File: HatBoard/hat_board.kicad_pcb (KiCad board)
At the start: 4 copper layers, 132 x 106.5 mm, 50 parts, among them J1 DF11 FC Connection, J13 DF11 FC Connection, J20 DF11 FC Connection, J21 DF11 FC Connection, J3 Conn_01x04, J4 Conn_01x04, J5 Conn_01x04, J6 Conn_01x04, J7 Conn_01x04, J8 Conn_01x04, U10 VEML7700, U12 DRV2605LDGS, U13 TCA4311A, U17 TCA4311A, U21 TCA4311A, U27 TMP112AIDRLR, U4 TCA4311A, U5 TCA4311A, U9 TCA4311A

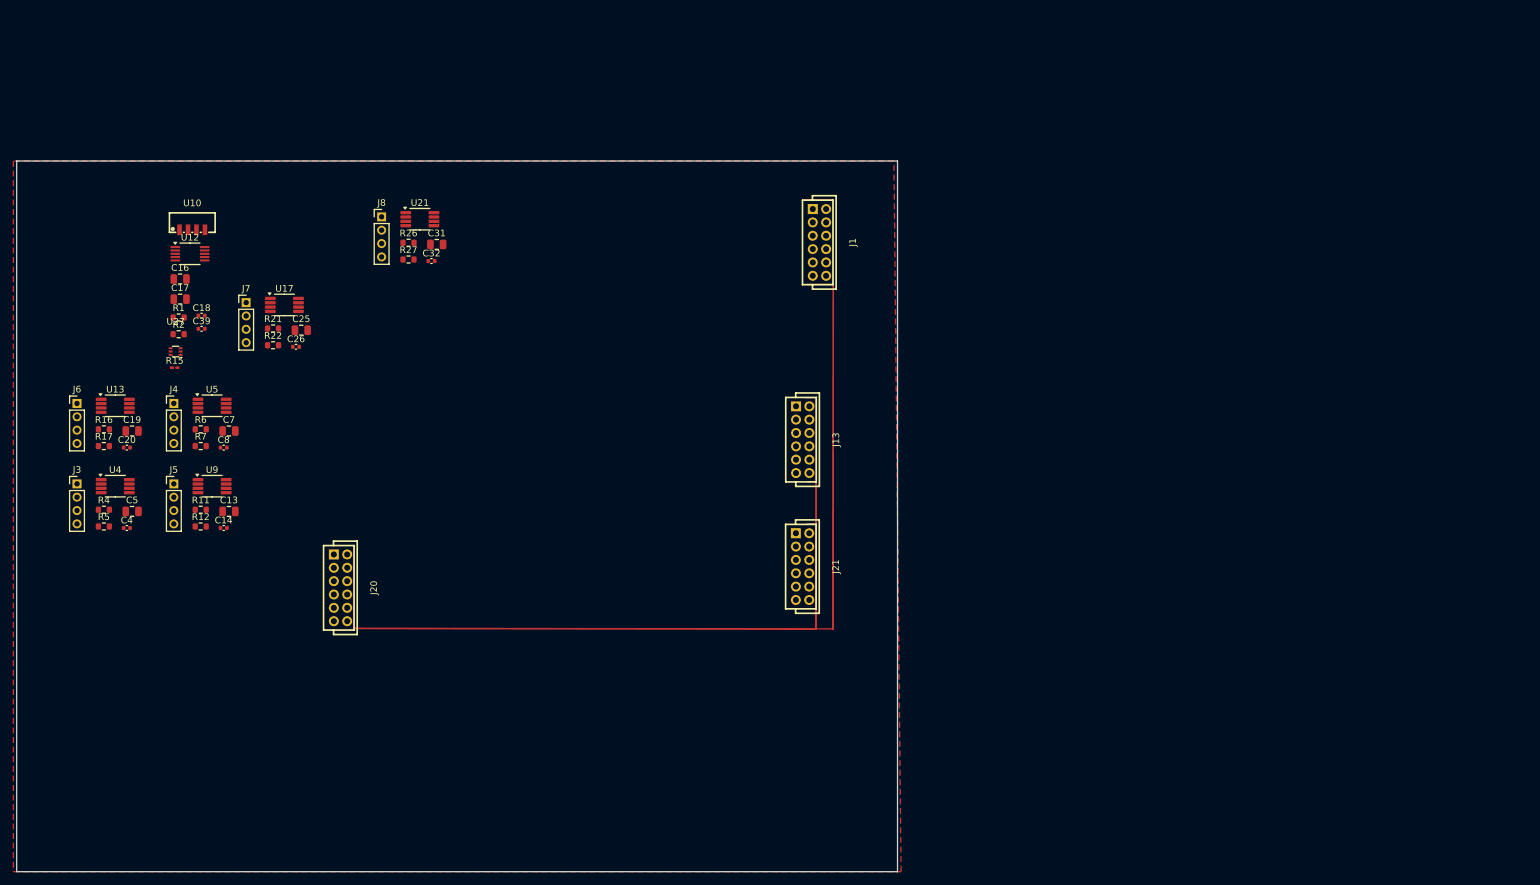
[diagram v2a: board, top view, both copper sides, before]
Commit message: mirror flipped placement
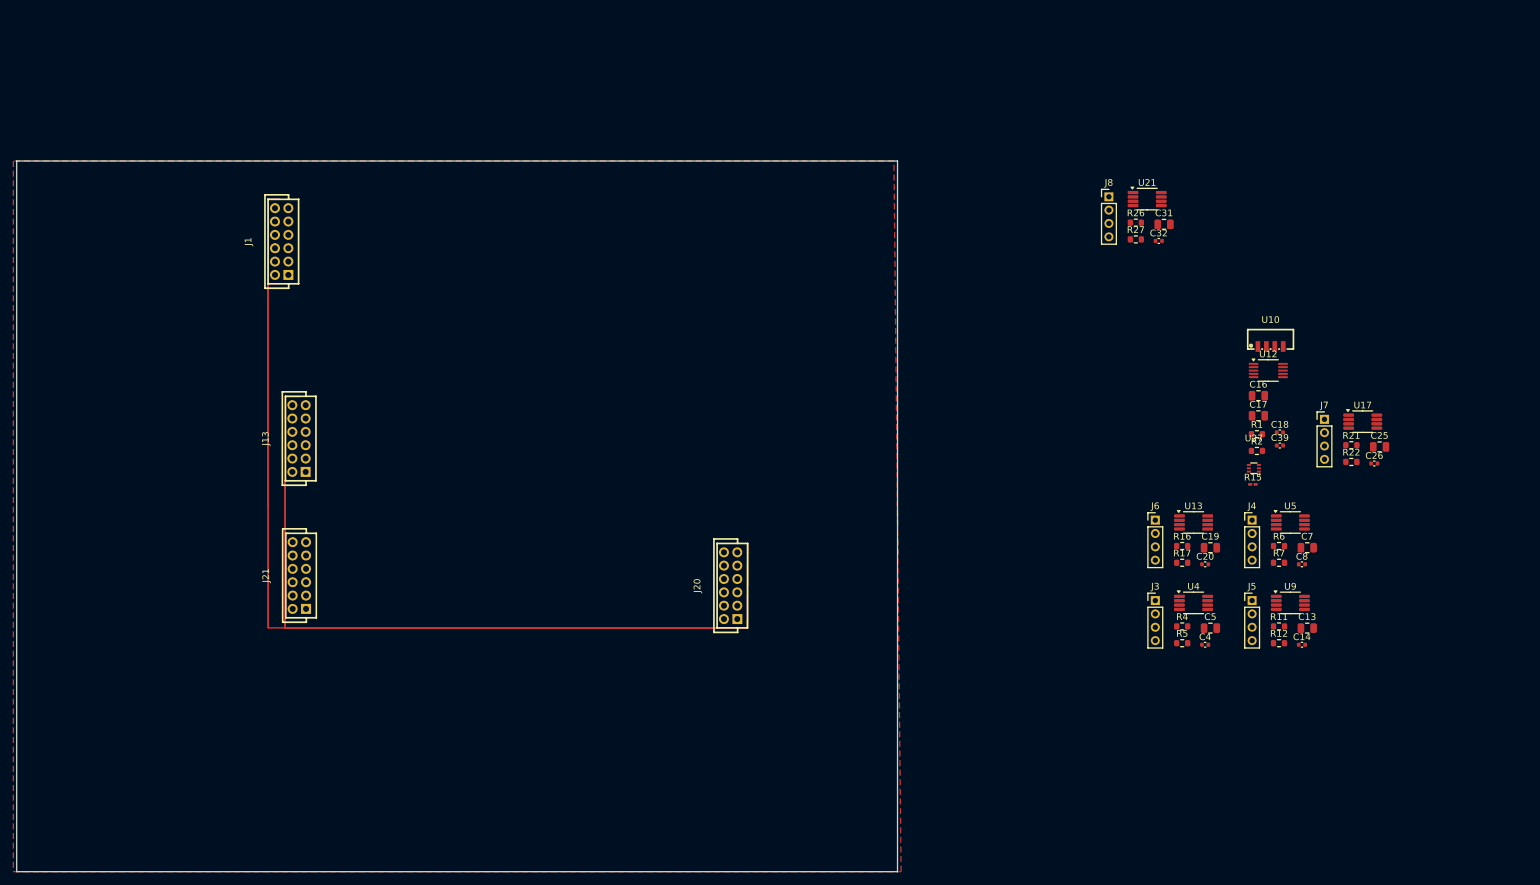
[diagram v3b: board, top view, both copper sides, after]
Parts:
- moved C14 162.5 mm to (223.1, 132.5)
- moved C17 162.5 mm to (216.6, 98.2)
- moved C25 162.5 mm to (234.7, 102.8)
- moved C4 162.5 mm to (208.6, 132.5)
- moved C7 162.5 mm to (223.9, 118.0)
- moved J3 162.5 mm to (201.1, 125.9)
- moved R16 162.5 mm to (205.2, 117.7)
- moved R2 162.5 mm to (216.4, 103.5)
- moved U17 162.5 mm to (232.2, 99.1)
- moved C13 162.5 mm to (223.9, 130.0)
- moved C16 162.5 mm to (216.6, 95.2)
- moved C18 162.5 mm to (219.8, 100.7)
- moved C19 162.5 mm to (209.4, 118.0)
- moved C20 162.5 mm to (208.6, 120.4)
- moved C39 162.5 mm to (219.8, 102.6)
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
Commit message: finihsed connection, need to reroute certain traces ++ double check orientation of connectors
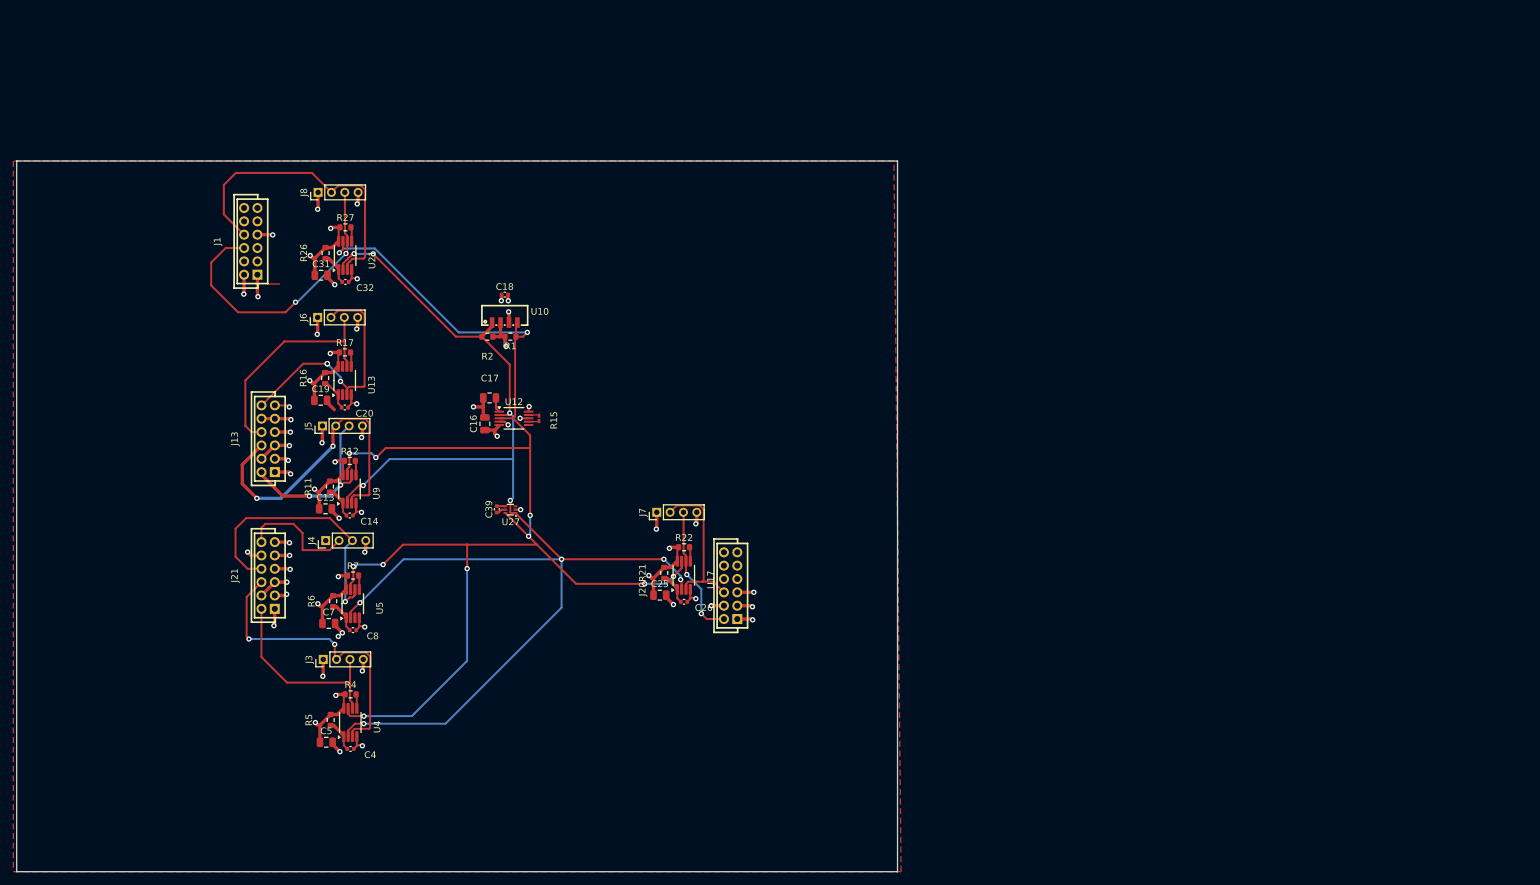
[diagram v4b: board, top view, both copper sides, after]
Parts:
- moved C13 148.2 mm to (76.8, 112.1)
- moved C7 147.1 mm to (77.3, 129.3)
- moved C14 144.0 mm to (80.4, 113.1)
- moved R11 143.8 mm to (77.4, 108.8), turned to -90 degrees
- moved C8 142.6 mm to (80.9, 130.3)
- moved U9 142.0 mm to (80.4, 109.2), turned to 90 degrees
- moved R6 142.0 mm to (77.9, 126.0), turned to -90 degrees
- moved R12 141.9 mm to (80.4, 104.9)
- moved J5 141.8 mm to (76.3, 99.7), turned to 90 degrees
- moved U5 141.0 mm to (80.9, 126.3), turned to 90 degrees
- moved J4 138.9 mm to (76.8, 116.9), turned to 90 degrees
- moved R7 138.8 mm to (80.9, 122.1)
- moved C19 135.1 mm to (76.1, 95.9)
- moved C5 133.6 mm to (76.9, 147.1)
- moved C20 131.1 mm to (79.7, 96.9)
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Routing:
- net SDA: track 0.00 -> 209.4 mm, vias 0 -> 12
- net SCL: track 0.00 -> 203.5 mm, vias 0 -> 10
- net +3V3: track 0.00 -> 109.5 mm, vias 0 -> 25
- net GND: track 0.00 -> 91.3 mm, vias 0 -> 40
- net /SCLIN: track 0.00 -> 68.1 mm, vias 0 -> 2
- net /SDAIN: track 0.00 -> 66.6 mm, vias 0 -> 2
- net /SCLIN_F3: track 0.00 -> 48.0 mm, vias 0 -> 2
- net /SCLIN_F1: track 0.00 -> 45.2 mm, vias 0 -> 2
- net /SDAIN_F2: track 0.00 -> 40.7 mm, vias 0 -> 1
- net /SCLIN_F4: track 0.00 -> 38.4 mm, vias 0 -> 3
- net /SCDAIN_F4: track 0.00 -> 34.4 mm
- net /SDAIN_F1: track 0.00 -> 29.6 mm
- net /SDAIN_F3: track 0.00 -> 27.3 mm, vias 0 -> 2
- net /SCLIN_F2: track 0.00 -> 17.7 mm
- net Net-(U9-EN): track 0.00 -> 4.80 mm
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
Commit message: corrected PCB design
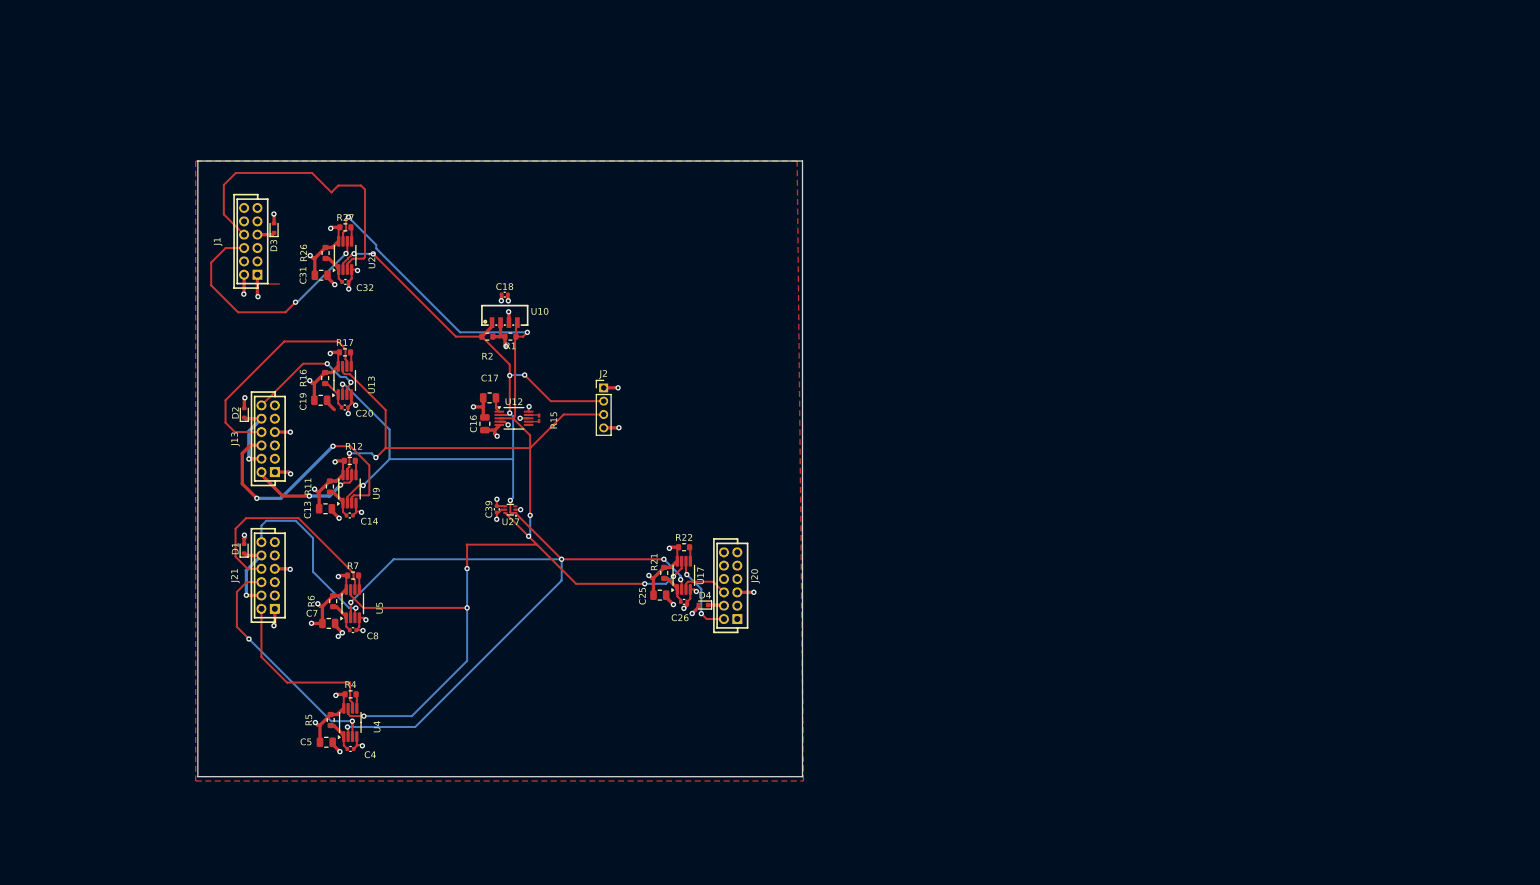
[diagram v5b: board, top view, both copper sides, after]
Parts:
- removed J3, J4, J5, J6, J7, J8: Conn_01x04, Connector_PinHeader_2.00mm:PinHeader_1x04_P2.00mm_Vertical
- added D1: 1N4148WT, Diode_SMD:D_SOD-523, F.Cu at (64.6, 118.1)
- added D2: 1N4148WT, Diode_SMD:D_SOD-523, F.Cu at (64.6, 97.8)
- added D3: 1N4148WT, Diode_SMD:D_SOD-523, F.Cu at (69.1, 70.1)
- added D4: 1N4148WT, Diode_SMD:D_SOD-523, F.Cu at (133.4, 126.5)
- added J2: Conn_01x04, Connector_PinHeader_2.00mm:PinHeader_1x04_P2.00mm_Vertical, F.Cu at (118.5, 94.0)
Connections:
- J1 pad 6: /SCLIN -> /SCLIN_ANT
- J1 pad 7: +3V3 -> Net-(D3-K)
- J1 pad 8: /SDAIN -> /SDAIN_ANT
- J13 pad 10: +3V3 -> Net-(D2-K)
- J13 pad 11: +3V3 -> unconnected-(J13-Pin_11-Pad11)
- J13 pad 3: GND -> unconnected-(J13-Pin_3-Pad3)
- J13 pad 4: +3V3 -> Net-(D2-K)
- J13 pad 5: +3V3 -> unconnected-(J13-Pin_5-Pad5)
- J13 pad 9: +3V3 -> unconnected-(J13-Pin_9-Pad9)
- J20 pad 1: GND -> unconnected-(J20-Pin_1-Pad1)
- J20 pad 2: /SDAIN -> /SDAINZ
- J20 pad 3: GND -> unconnected-(J20-Pin_3-Pad3)
- J20 pad 4: +3V3 -> Net-(D4-K)
- J20 pad 6: /SCLIN -> /SCLINZ
- J21 pad 10: +3V3 -> Net-(D1-K)
- J21 pad 11: +3V3 -> unconnected-(J21-Pin_11-Pad11)
- J21 pad 3: GND -> unconnected-(J21-Pin_3-Pad3)
- J21 pad 4: +3V3 -> Net-(D1-K)
- J21 pad 5: +3V3 -> unconnected-(J21-Pin_5-Pad5)
- J21 pad 9: +3V3 -> unconnected-(J21-Pin_9-Pad9)
- U17 pad 3: /SCLIN -> /SCLINZ
- U17 pad 6: /SDAIN -> /SDAINZ
- U21 pad 3: /SDAIN -> /SDAIN_ANT
- U21 pad 6: /SCLIN -> /SCLIN_ANT
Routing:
- net /SCLIN: track 68.1 -> 0.00 mm, vias 2 -> 0
- net /SDAIN: track 66.6 -> 0.00 mm, vias 2 -> 0
- net /SDAIN_ANT: track 0.00 -> 46.5 mm
- net /SCLIN_ANT: track 0.00 -> 36.7 mm, vias 0 -> 2
- net SCL: track 203.5 -> 234.0 mm, vias 10 -> 13
- net SDA: track 209.4 -> 237.7 mm, vias 12 -> 11
- net GND: track 91.3 -> 70.3 mm, vias 40 -> 32
- net +3V3: track 109.5 -> 90.8 mm, vias 25 -> 22
- net /SCLIN_F4: track 38.4 -> 20.1 mm, vias 3 -> 2
- net /SDAINZ: track 0.00 -> 12.5 mm, vias 0 -> 2
- net Net-(D1-K): track 0.00 -> 11.9 mm, vias 0 -> 1
- net Net-(D2-K): track 0.00 -> 11.4 mm, vias 0 -> 1
- net /SCLIN_F1: track 45.2 -> 35.0 mm
- net /SDAIN_F3: track 27.3 -> 17.9 mm
- net /SCLIN_F2: track 17.7 -> 26.8 mm, vias 0 -> 1
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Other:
- board size 132 x 106.5 mm -> 90.6 x 92.3 mm

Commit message: diode added
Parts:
- removed J1, J13, J20, J21: DF11 FC Connection, easyeda2kicad:CONN-TH_DF11-12DS-2DSA-05
- added H1: MountingHole, MountingHole:MountingHole_3.2mm_M3_DIN965_Pad, F.Cu at (169.2, 129.1)
- added H2: MountingHole, MountingHole:MountingHole_3.2mm_M3_DIN965_Pad, F.Cu at (249.2, 129.1)
- added J3: Z-DF11 FC Connection, easyeda2kicad:CONN-TH_DF11-12DS-2DSA-05, B.Cu at (173.3, 110.9)
- added J4: DF11 FC Connection, easyeda2kicad:CONN-TH_DF11-12DS-2DSA-05, B.Cu at (245.1, 59.3)
- added J5: DF11 FC Connection, easyeda2kicad:CONN-TH_DF11-12DS-2DSA-05, B.Cu at (245.1, 101.3)
- added J6: DF11 FC Connection, easyeda2kicad:CONN-TH_DF11-12DS-2DSA-05, B.Cu at (245.2, 86.3)
- D1, D2, D3, D4: value 1N4148WT -> D_Schottky; footprint Diode_SMD:D_SOD-523 -> easyeda2kicad:POWERDI-123_L2.8-W1.8-LS3.7-RD
- moved D2 188.3 mm to (247.0, 50.9), turned to 180 degrees
- moved C5 184.4 mm to (246.2, 74.2)
- moved C4 179.7 mm to (245.4, 76.7)
- moved U4 179.1 mm to (243.7, 70.4), turned to 0 degrees
- moved R5 177.7 mm to (242.0, 76.4), turned to 0 degrees
- moved R4 174.4 mm to (242.0, 73.9)
- moved D3 174.0 mm to (239.7, 104.3), turned to 180 degrees
- moved C19 170.6 mm to (245.5, 116.1)
- moved C20 166.5 mm to (244.7, 118.6)
- moved C7 166.3 mm to (238.0, 86.8)
- moved R16 166.2 mm to (241.3, 115.9), turned to 0 degrees
- moved U13 164.5 mm to (243.0, 112.3), turned to 0 degrees
- moved R17 164.3 mm to (241.3, 118.4)
- moved C31 163.8 mm to (239.0, 60.0)
- moved C13 161.8 mm to (238.0, 99.0)
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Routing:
- net SDA: track 237.7 -> 2.57 mm, vias 11 -> 0
- net SCL: track 234.0 -> 2.59 mm, vias 13 -> 0
- net +3V3: track 90.8 -> 9.45 mm, vias 22 -> 4
- net GND: track 70.3 -> 12.7 mm, vias 32 -> 3
- net /SDAIN_ANT: track 46.5 -> 0.00 mm
- net /SCLIN_F3: track 40.4 -> 0.07 mm, vias 2 -> 0
- net /SCLIN_ANT: track 36.7 -> 0.00 mm, vias 2 -> 0
- net /SCLIN_F1: track 35.0 -> 0.71 mm, vias 2 -> 0
- net /SCDAIN_F4: track 34.2 -> 0.52 mm
- net /SDAIN_F2: track 33.6 -> 0.00 mm
- net /SCLIN_F2: track 26.8 -> 0.00 mm, vias 1 -> 0
- net /SDAIN_F1: track 26.1 -> 0.00 mm
- net /SCLIN_F4: track 20.1 -> 0.00 mm, vias 2 -> 0
- net /SDAIN_F3: track 17.9 -> 0.00 mm, vias 2 -> 0
- net Net-(D1-K): track 11.9 -> 0.00 mm, vias 1 -> 0
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- added copper zone on F.Cu, net (none)
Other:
- board size 90.6 x 92.3 mm -> 88 x 94.5 mm
- board text added: "Antenna Board"

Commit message: connect
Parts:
- moved R27 6.37 mm to (240.0, 58.7), turned to 180 degrees
- moved R4 5.81 mm to (240.6, 79.6), turned to 90 degrees
- moved U4 5.41 mm to (243.0, 75.7), turned to -90 degrees
- moved C4 5.34 mm to (243.1, 71.8), turned to 180 degrees
- moved R5 4.47 mm to (245.9, 74.2), turned to 90 degrees
- moved C5 4.05 mm to (246.9, 78.2)
- moved C32 2.58 mm to (237.2, 60.1), turned to -90 degrees
- moved D4 1.36 mm to (240.8, 83.2)
- moved C31 1.05 mm to (239.7, 60.8), turned to 180 degrees
- moved C18 0.80 mm to (209.7, 69.4)
- moved U10 0.80 mm to (209.7, 67.8)
- moved D3 0.20 mm to (239.8, 104.1)
- moved C39 0.07 mm to (203.2, 95.7)
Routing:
- net SCL: track 2.59 -> 85.7 mm, vias 0 -> 3
- net SDA: track 2.57 -> 76.7 mm, vias 0 -> 2
- net +3V3: track 9.45 -> 53.5 mm, vias 4 -> 15
- net GND: track 12.7 -> 31.1 mm, vias 3 -> 11
- net /SCLIN_F1: track 0.71 -> 12.3 mm, vias 0 -> 1
- net /SDAIN_ANT: track 0.00 -> 11.3 mm
- net /SDAIN_F2: track 0.00 -> 11.1 mm
- net Net-(D2-K): track 0.00 -> 10.3 mm
- net Net-(D4-K): track 0.07 -> 10.2 mm
- net Net-(D1-K): track 0.00 -> 9.49 mm, vias 0 -> 1
- net /SCLIN_ANT: track 0.00 -> 6.24 mm
- net /SDAIN_F1: track 0.00 -> 4.08 mm
- net Net-(U17-READY): track 0.00 -> 4.05 mm
- net Net-(U4-EN): track 0.00 -> 3.95 mm
- net Net-(U4-READY): track 0.00 -> 1.73 mm
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
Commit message: no electrical errors added cake:
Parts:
- added Cake!: LOGO, LOGO, F.Cu at (195.9, 55.6)
- moved C20 17.3 mm to (232.1, 106.8), turned to -90 degrees
- moved R16 13.4 mm to (234.7, 104.2), turned to 180 degrees
- moved C19 12.5 mm to (234.7, 109.9), turned to 180 degrees
- moved R17 11.6 mm to (241.0, 106.8), turned to -90 degrees
- moved C8 9.33 mm to (230.7, 82.7), turned to -90 degrees
- moved R12 9.03 mm to (241.3, 96.3), turned to -90 degrees
- moved U13 8.75 mm to (236.1, 106.9)
- moved R7 7.77 mm to (238.8, 83.2), turned to -90 degrees
- moved C14 6.57 mm to (233.0, 96.5), turned to -90 degrees
- moved R11 6.30 mm to (237.0, 93.4), turned to 180 degrees
- moved R6 6.20 mm to (233.9, 80.4), turned to 180 degrees
- moved C7 4.69 mm to (233.3, 86.4), turned to 180 degrees
- moved C13 2.34 mm to (235.7, 99.2), turned to 180 degrees
- moved U9 1.71 mm to (237.0, 96.1)
- moved U5 0.89 mm to (234.6, 83.2)
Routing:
- net SDA: track 76.7 -> 174.0 mm, vias 2 -> 6
- net SCL: track 85.7 -> 182.5 mm, vias 3 -> 12
- net GND: track 31.1 -> 64.9 mm, vias 11 -> 21
- net +3V3: track 53.5 -> 74.0 mm, vias 15 -> 23
- net /SCLIN_F2: track 0.00 -> 13.2 mm, vias 0 -> 1
- net /SCLIN_F4: track 0.00 -> 12.8 mm, vias 0 -> 1
- net Net-(D3-K): track 0.00 -> 12.2 mm, vias 0 -> 2
- net /SCLIN_F3: track 0.07 -> 10.9 mm
- net Net-(U21-EN): track 1.71 -> 12.1 mm, vias 0 -> 2
- net /SCDAIN_F4: track 0.52 -> 6.74 mm
- net Net-(U13-EN): track 0.00 -> 5.45 mm
- net /SDAIN_F3: track 0.00 -> 5.03 mm
- net Net-(U9-EN): track 0.00 -> 4.50 mm
- net Net-(U5-EN): track 0.00 -> 3.88 mm
- net /SDAIN_F2: track 11.1 -> 14.0 mm, vias 0 -> 1
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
